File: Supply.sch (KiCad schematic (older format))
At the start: 22 parts, among them IC2 TPS65320C

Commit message: - removed 1 MOSFET of each group (no space) - removed 2 DC buffer caps (no space) - power stage routed - shunts and amps routed - post driver routed - pre driver HV routed
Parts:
- removed B1: MTC1, alexmod:MTC1, symbol MTC1
- removed C28: 22u, Capacitors_SMD:C_1206, symbol C
- removed C46: 5n6, Capacitors_SMD:C_0805, symbol C
- removed C47: 10u, Capacitors_SMD:C_0805, symbol C
- removed D8, D9: D_Schottky, Diodes_SMD:SMA_Standard, symbol D_Schottky
- removed IC2: TPS65320C, alexmod:TSSOP-14_4.4x5mm_Pitch0.65mm_EP, symbol TPS65320C
- added C10: 22u, Capacitors_SMD:C_0805, symbol C
- added C11, C12: 100n, Capacitors_SMD:C_0805, symbol C
- added C28: 100n, Capacitors_SMD:C_0805, symbol C_Small
- added C46: 3n3, Capacitors_SMD:C_0805, symbol C_Small
- added D8: 4148, Diodes_SMD:D_MiniMELF_Standard, symbol D_Small
- added IC1: LM5017, Housings_SOIC:SOIC-8-1EP_3.9x4.9mm_Pitch1.27mm, symbol LM5017
- added IC2: AP65111, TO_SOT_Packages_SMD:SOT-23-6, symbol AP65111
- added L2: NRH2410T100MN, alexmod:NRH2410, symbol INDUCTOR_SMALL
- added R30: 76k, Resistors_SMD:R_0805, symbol R
- added R31: 10k, Resistors_SMD:R_0805, symbol R
- added R49: 13k, Resistors_SMD:R_0805, symbol R
- added U6: 7805_SO8, Housings_SOIC:SOIC-8_3.9x4.9mm_Pitch1.27mm, symbol 7805_SO8
- C27: value 22u -> 100n; footprint Capacitors_SMD:C_1206 -> Capacitors_SMD:C_0805
- C29: value 100u 16V -> 47u 120V; footprint Capacitors_ThroughHole:C_Radial_D6.3_L11.2_P2.5 -> Capacitors_THT:CP_Radial_D6.3mm_P2.50mm
- C31: value 3n3 -> 100n
- C45: value 10p -> 22u
- C48: value 10u -> 22u
- C49: value 100u 6V3 -> 100u 22V; footprint Capacitors_ThroughHole:C_Radial_D6.3_L11.2_P2.5 -> Capacitors_THT:CP_Radial_D6.3mm_P2.50mm
- L1: value SRR6038-3R3Y -> VLS6045EX-221M; footprint alexmod:SRR6038 -> alexmod:VLS6045EX
- R39: value 52k3 -> 499k
- R40: value 28k -> 59k
- R41: value 30k1 -> 46k4
- R42: value 95k3 -> 40k2
- R43: value 18k2 -> 1k
- R44: value 95k3 -> 10k
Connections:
- net labels removed: +12VA, Earth, NRST
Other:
- moved on the sheet: C29, C30, C31, C32, C48, C49, L1, R43, R44

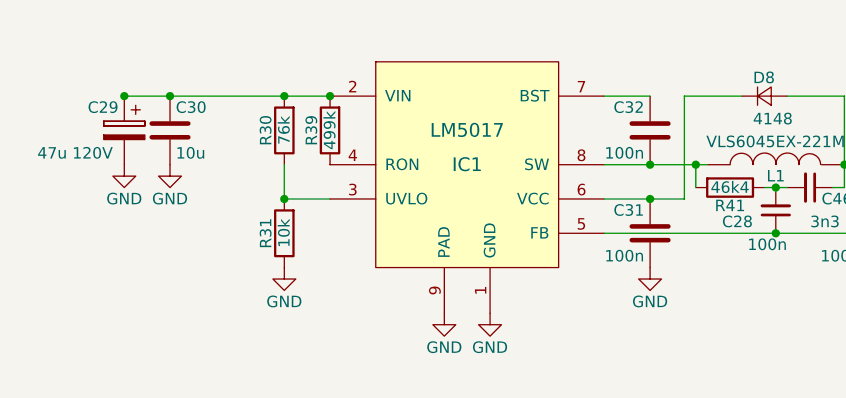
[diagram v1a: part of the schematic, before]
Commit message: - redesigned the MOSFET mounting -> minor changes to the power stage - logic and interface routed -> layout finished - needs final check and gerber export
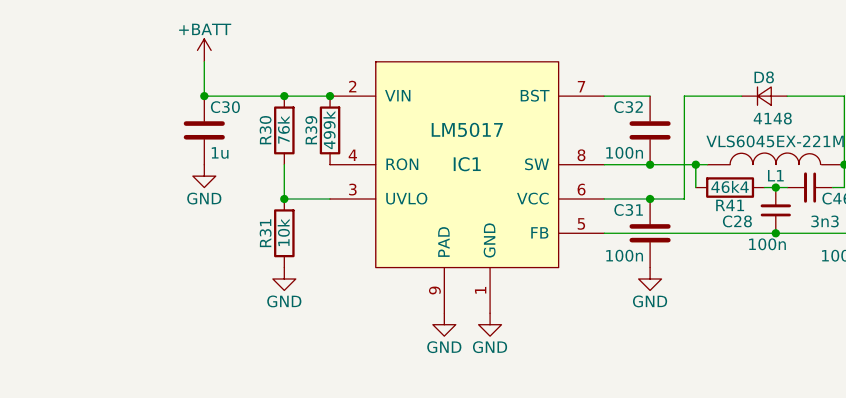
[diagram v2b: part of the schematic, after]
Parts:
- removed C29: 47u 120V, Capacitors_THT:CP_Radial_D6.3mm_P2.50mm, symbol CP
- C30: value 10u -> 1u; footprint Capacitors_SMD:C_0805 -> Capacitors_SMD:C_1206
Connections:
- net +BATT: now reaches C30.1, IC1.2 (VIN), R30.2, R39.2
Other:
- moved on the sheet: C30
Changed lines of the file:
@@
 L C C30
 U 1 1 589B52B3
-P 3750 1600
-F 0 "C30" H 3775 1700 50  0000 L CNN
-F 1 "10u" H 3775 1500 50  0000 L CNN
-F 2 "Capacitors_SMD:C_0805" H 3788 1450 50  0001 C CNN
-F 3 "" H 3750 1600 50  0000 C CNN
-	1    3750 1600
-	1    0    0    -1
-$EndComp
-$Comp
-L CP C29
-U 1 1 589B52D8
-P 3550 1600
-F 0 "C29" H 3575 1700 50  0000 L CNN
-F 1 "47u 120V" H 3600 1500 50  0000 L CNN
-F 2 "Capacitors_THT:CP_Radial_D6.3mm_P2.50mm" H 3588 1450 50  0001 C CNN
-F 3 "" H 3550 1600 50  0000 C CNN
-	1    3550 1600
-	-1   0    0    -1
+P 3900 1600
+F 0 "C30" H 3925 1700 50  0000 L CNN
+F 1 "1u" H 3925 1500 50  0000 L CNN
+F 2 "Capacitors_SMD:C_1206" H 3938 1450 50  0001 C CNN
+F 3 "" H 3900 1600 50  0000 C CNN
+	1    3900 1600
+	1    0    0    -1
 $EndComp
 $Comp
@@
 Connection ~ 7500 1750
 Wire Wire Line
-	3550 1450 4450 1450
-Connection ~ 3750 1450
-Connection ~ 3550 1450
+	3900 1450 4450 1450
+Connection ~ 3900 1450
 $Comp
 L GND #PWR054
 U 1 1 59A204D9
-P 3750 1750
-F 0 "#PWR054" H 3750 1500 50  0001 C CNN
-F 1 "GND" H 3750 1600 50  0000 C CNN
-F 2 "" H 3750 1750 60  0000 C CNN
-F 3 "" H 3750 1750 60  0000 C CNN
-	1    3750 1750
+P 3900 1750
+F 0 "#PWR054" H 3900 1500 50  0001 C CNN
+F 1 "GND" H 3900 1600 50  0000 C CNN
+F 2 "" H 3900 1750 60  0000 C CNN
+F 3 "" H 3900 1750 60  0000 C CNN
+	1    3900 1750
 	1    0    0    -1
 $EndComp
 $Comp
 L GND #PWR055
-U 1 1 59A20552
-P 3550 1750
-F 0 "#PWR055" H 3550 1500 50  0001 C CNN
-F 1 "GND" H 3550 1600 50  0000 C CNN
-F 2 "" H 3550 1750 60  0000 C CNN
-F 3 "" H 3550 1750 60  0000 C CNN
-	1    3550 1750
-	1    0    0    -1
-$EndComp
-$Comp
-L GND #PWR056
 U 1 1 59A20BA8
 P 5150 2400
-F 0 "#PWR056" H 5150 2150 50  0001 C CNN
+F 0 "#PWR055" H 5150 2150 50  0001 C CNN
 F 1 "GND" H 5150 2250 50  0000 C CNN
 F 2 "" H 5150 2400 60  0000 C CNN
@@
 Connection ~ 4450 1450
 $Comp
-L GND #PWR057
+L GND #PWR056
 U 1 1 59A21253
 P 4950 2400
-F 0 "#PWR057" H 4950 2150 50  0001 C CNN
+F 0 "#PWR056" H 4950 2150 50  0001 C CNN
 F 1 "GND" H 4950 2250 50  0000 C CNN
 F 2 "" H 4950 2400 60  0000 C CNN
@@
 	4250 1900 4450 1900
 $Comp
-L GND #PWR058
+L GND #PWR057
 U 1 1 59A21882
 P 4250 2200
-F 0 "#PWR058" H 4250 1950 50  0001 C CNN
+F 0 "#PWR057" H 4250 1950 50  0001 C CNN
 F 1 "GND" H 4250 2050 50  0000 C CNN
 F 2 "" H 4250 2200 60  0000 C CNN
@@
 	6250 1450 6000 1450
 Wire Wire Line
-	6000 1450 6000 1900
-Wire Wire Line
-	6000 1900 5650 1900
+	6000 1900 6000 1450
+Wire Wire Line
+	5650 1900 6000 1900
 $Comp
 L AP65111 IC2
@@
 $EndComp
 $Comp
-L +12V #PWR059
+L +12V #PWR058
 U 1 1 59A25AAF
 P 4300 3500
-F 0 "#PWR059" H 4300 3350 50  0001 C CNN
+F 0 "#PWR058" H 4300 3350 50  0001 C CNN
 F 1 "+12V" H 4300 3640 50  0000 C CNN
 F 2 "" H 4300 3500 60  0000 C CNN
@@
 Connection ~ 4300 3600
 $Comp
-L GND #PWR060
+L GND #PWR059
 U 1 1 59A26187
 P 4300 3900
-F 0 "#PWR060" H 4300 3650 50  0001 C CNN
+F 0 "#PWR059" H 4300 3650 50  0001 C CNN
 F 1 "GND" H 4300 3750 50  0000 C CNN
 F 2 "" H 4300 3900 60  0000 C CNN
@@
 $EndComp
 $Comp
-L GND #PWR061
+L GND #PWR060
 U 1 1 59A26636
 P 5050 4200
-F 0 "#PWR061" H 5050 3950 50  0001 C CNN
+F 0 "#PWR060" H 5050 3950 50  0001 C CNN
 F 1 "GND" H 5050 4050 50  0000 C CNN
 F 2 "" H 5050 4200 50  0000 C CNN
@@
 $EndComp
 $Comp
-L GND #PWR062
+L GND #PWR061
 U 1 1 59A2668D
 P 6200 4200
-F 0 "#PWR062" H 6200 3950 50  0001 C CNN
+F 0 "#PWR061" H 6200 3950 50  0001 C CNN
 F 1 "GND" H 6200 4050 50  0000 C CNN
 F 2 "" H 6200 4200 50  0000 C CNN
@@
 $EndComp
 $Comp
-L GND #PWR063
+L GND #PWR062
 U 1 1 59A26802
 P 6500 4200
-F 0 "#PWR063" H 6500 3950 50  0001 C CNN
+F 0 "#PWR062" H 6500 3950 50  0001 C CNN
 F 1 "GND" H 6500 4050 50  0000 C CNN
 F 2 "" H 6500 4200 50  0000 C CNN
@@
 Connection ~ 5500 3600
 $Comp
-L +3V3 #PWR064
+L +3V3 #PWR063
 U 1 1 59A27760
 P 6500 3500
-F 0 "#PWR064" H 6500 3350 50  0001 C CNN
+F 0 "#PWR063" H 6500 3350 50  0001 C CNN
 F 1 "+3V3" H 6500 3640 50  0000 C CNN
 F 2 "" H 6500 3500 50  0000 C CNN
@@
 Connection ~ 6500 3600
 $Comp
-L +12V #PWR065
+L +12V #PWR064
 U 1 1 59A27DFE
 P 4600 5050
-F 0 "#PWR065" H 4600 4900 50  0001 C CNN
+F 0 "#PWR064" H 4600 4900 50  0001 C CNN
 F 1 "+12V" H 4600 5190 50  0000 C CNN
 F 2 "" H 4600 5050 60  0000 C CNN
@@
 Connection ~ 4600 5150
 $Comp
-L GND #PWR066
+L GND #PWR065
 U 1 1 59A27E0D
 P 4600 5450
-F 0 "#PWR066" H 4600 5200 50  0001 C CNN
+F 0 "#PWR065" H 4600 5200 50  0001 C CNN
 F 1 "GND" H 4600 5300 50  0000 C CNN
 F 2 "" H 4600 5450 60  0000 C CNN
@@
 Connection ~ 5550 5150
 $Comp
-L GND #PWR067
+L GND #PWR066
 U 1 1 59A2862B
 P 5550 5450
-F 0 "#PWR067" H 5550 5200 50  0001 C CNN
+F 0 "#PWR066" H 5550 5200 50  0001 C CNN
 F 1 "GND" H 5550 5300 50  0000 C CNN
 F 2 "" H 5550 5450 60  0000 C CNN
@@
 $EndComp
 $Comp
-L GND #PWR068
+L GND #PWR067
 U 1 1 59A28C15
 P 5100 5450
-F 0 "#PWR068" H 5100 5200 50  0001 C CNN
+F 0 "#PWR067" H 5100 5200 50  0001 C CNN
 F 1 "GND" H 5100 5300 50  0000 C CNN
 F 2 "" H 5100 5450 60  0000 C CNN
@@
 $EndComp
 $Comp
-L GND #PWR069
+L GND #PWR068
 U 1 1 59BF9EB5
 P 4950 5450
-F 0 "#PWR069" H 4950 5200 50  0001 C CNN
+F 0 "#PWR068" H 4950 5200 50  0001 C CNN
 F 1 "GND" H 4950 5300 50  0000 C CNN
 F 2 "" H 4950 5450 60  0000 C CNN
@@
 $EndComp
 $Comp
-L GND #PWR070
+L GND #PWR069
 U 1 1 59BF9F14
 P 5000 5450
-F 0 "#PWR070" H 5000 5200 50  0001 C CNN
+F 0 "#PWR069" H 5000 5200 50  0001 C CNN
 F 1 "GND" H 5000 5300 50  0000 C CNN
 F 2 "" H 5000 5450 60  0000 C CNN
@@
 $EndComp
 $Comp
-L GND #PWR071
+L GND #PWR070
 U 1 1 59BFA02F
 P 5150 5450
-F 0 "#PWR071" H 5150 5200 50  0001 C CNN
+F 0 "#PWR070" H 5150 5200 50  0001 C CNN
 F 1 "GND" H 5150 5300 50  0000 C CNN
 F 2 "" H 5150 5450 60  0000 C CNN
@@
 	-1   0    0    -1
 $EndComp
+$Comp
+L +BATT #PWR071
+U 1 1 59C14A31
+P 3900 1300
+F 0 "#PWR071" H 3900 1150 50  0001 C CNN
+F 1 "+BATT" H 3900 1440 50  0000 C CNN
+F 2 "" H 3900 1300 50  0000 C CNN
+F 3 "" H 3900 1300 50  0000 C CNN
+	1    3900 1300
+	1    0    0    -1
+$EndComp
+Wire Wire Line
+	3900 1300 3900 1450
 $EndSCHEMATC

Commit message: - final check - minor layout cleanups - labeling - first production run => V1.0
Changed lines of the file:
@@
 	6250 1450 6000 1450
 Wire Wire Line
-	6000 1900 6000 1450
+	6000 1450 6000 1900
 Wire Wire Line
-	5650 1900 6000 1900
+	6000 1900 5650 1900
 $Comp
 L AP65111 IC2

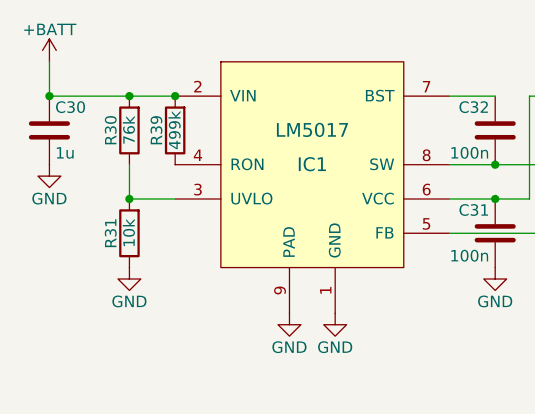
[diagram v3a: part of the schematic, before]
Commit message: - fixed swapped pins 2 and 3 on IC2 - added optional dividers to ADC inputs - made Vcc selectable between 3V3 or 5V
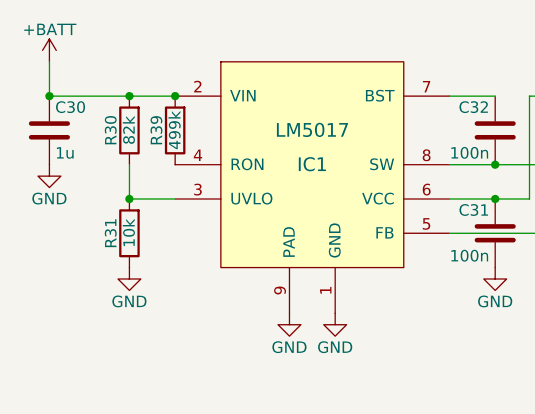
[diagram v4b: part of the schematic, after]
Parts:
- R30: value 76k -> 82k
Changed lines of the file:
@@
 $EndDescr
 $Comp
-L +12V #PWR048
+L +12V #PWR051
 U 1 1 5757C6C9
 P 7500 1650
-F 0 "#PWR048" H 7500 1500 50  0001 C CNN
+F 0 "#PWR051" H 7500 1500 50  0001 C CNN
 F 1 "+12V" H 7500 1790 50  0000 C CNN
 F 2 "" H 7500 1650 60  0000 C CNN
@@
 $EndComp
 $Comp
-L GND #PWR049
+L GND #PWR052
 U 1 1 589B6D8B
 P 5850 2200
-F 0 "#PWR049" H 5850 1950 50  0001 C CNN
+F 0 "#PWR052" H 5850 1950 50  0001 C CNN
 F 1 "GND" H 5850 2050 50  0000 C CNN
 F 2 "" H 5850 2200 60  0000 C CNN
@@
 $EndComp
 $Comp
-L +5V #PWR050
+L +5V #PWR053
 U 1 1 589BAA8C
 P 5550 5050
-F 0 "#PWR050" H 5550 4900 50  0001 C CNN
+F 0 "#PWR053" H 5550 4900 50  0001 C CNN
 F 1 "+5V" H 5550 5190 50  0000 C CNN
 F 2 "" H 5550 5050 50  0000 C CNN
@@
 Connection ~ 6950 1750
 $Comp
-L GND #PWR051
+L GND #PWR054
 U 1 1 59A1EBF8
 P 6950 2200
-F 0 "#PWR051" H 6950 1950 50  0001 C CNN
+F 0 "#PWR054" H 6950 1950 50  0001 C CNN
 F 1 "GND" H 6950 2050 50  0000 C CNN
 F 2 "" H 6950 2200 60  0000 C CNN
@@
 $EndComp
 $Comp
-L GND #PWR052
+L GND #PWR055
 U 1 1 59A1EC3C
 P 7200 2200
-F 0 "#PWR052" H 7200 1950 50  0001 C CNN
+F 0 "#PWR055" H 7200 1950 50  0001 C CNN
 F 1 "GND" H 7200 2050 50  0000 C CNN
 F 2 "" H 7200 2200 60  0000 C CNN
@@
 $EndComp
 $Comp
-L GND #PWR053
+L GND #PWR056
 U 1 1 59A1F45A
 P 7500 2350
-F 0 "#PWR053" H 7500 2100 50  0001 C CNN
+F 0 "#PWR056" H 7500 2100 50  0001 C CNN
 F 1 "GND" H 7500 2200 50  0000 C CNN
 F 2 "" H 7500 2350 60  0000 C CNN
@@
 Connection ~ 3900 1450
 $Comp
-L GND #PWR054
+L GND #PWR057
 U 1 1 59A204D9
 P 3900 1750
-F 0 "#PWR054" H 3900 1500 50  0001 C CNN
+F 0 "#PWR057" H 3900 1500 50  0001 C CNN
 F 1 "GND" H 3900 1600 50  0000 C CNN
 F 2 "" H 3900 1750 60  0000 C CNN
@@
 $EndComp
 $Comp
-L GND #PWR055
+L GND #PWR058
 U 1 1 59A20BA8
 P 5150 2400
-F 0 "#PWR055" H 5150 2150 50  0001 C CNN
+F 0 "#PWR058" H 5150 2150 50  0001 C CNN
 F 1 "GND" H 5150 2250 50  0000 C CNN
 F 2 "" H 5150 2400 60  0000 C CNN
@@
 Connection ~ 4450 1450
 $Comp
-L GND #PWR056
+L GND #PWR059
 U 1 1 59A21253
 P 4950 2400
-F 0 "#PWR056" H 4950 2150 50  0001 C CNN
+F 0 "#PWR059" H 4950 2150 50  0001 C CNN
 F 1 "GND" H 4950 2250 50  0000 C CNN
 F 2 "" H 4950 2400 60  0000 C CNN
@@
 P 4250 1600
 F 0 "R30" V 4330 1600 50  0000 C CNN
-F 1 "76k" V 4250 1600 50  0000 C CNN
+F 1 "82k" V 4250 1600 50  0000 C CNN
 F 2 "Resistors_SMD:R_0805" V 4180 1600 50  0001 C CNN
 F 3 "" H 4250 1600 50  0000 C CNN
@@
 	4250 1900 4450 1900
 $Comp
-L GND #PWR057
+L GND #PWR060
 U 1 1 59A21882
 P 4250 2200
-F 0 "#PWR057" H 4250 1950 50  0001 C CNN
+F 0 "#PWR060" H 4250 1950 50  0001 C CNN
 F 1 "GND" H 4250 2050 50  0000 C CNN
 F 2 "" H 4250 2200 60  0000 C CNN
@@
 	6000 1900 5650 1900
 $Comp
-L AP65111 IC2
-U 1 1 59A255A2
-P 5050 3600
-F 0 "IC2" H 5050 3500 60  0000 C CNN
-F 1 "AP65111" H 5050 3750 60  0000 C CNN
-F 2 "TO_SOT_Packages_SMD:SOT-23-6" H 5050 3400 60  0001 C CNN
-F 3 "" H 5050 3400 60  0000 C CNN
-	1    5050 3600
-	1    0    0    -1
-$EndComp
-$Comp
-L +12V #PWR058
+L +12V #PWR061
 U 1 1 59A25AAF
 P 4300 3500
-F 0 "#PWR058" H 4300 3350 50  0001 C CNN
+F 0 "#PWR061" H 4300 3350 50  0001 C CNN
 F 1 "+12V" H 4300 3640 50  0000 C CNN
 F 2 "" H 4300 3500 60  0000 C CNN
@@
 Connection ~ 4300 3600
 $Comp
-L GND #PWR059
+L GND #PWR062
 U 1 1 59A26187
 P 4300 3900
-F 0 "#PWR059" H 4300 3650 50  0001 C CNN
+F 0 "#PWR062" H 4300 3650 50  0001 C CNN
 F 1 "GND" H 4300 3750 50  0000 C CNN
 F 2 "" H 4300 3900 60  0000 C CNN
@@
 $EndComp
 $Comp
-L GND #PWR060
+L GND #PWR063
 U 1 1 59A26636
 P 5050 4200
-F 0 "#PWR060" H 5050 3950 50  0001 C CNN
+F 0 "#PWR063" H 5050 3950 50  0001 C CNN
 F 1 "GND" H 5050 4050 50  0000 C CNN
 F 2 "" H 5050 4200 50  0000 C CNN
@@
 $EndComp
 $Comp
-L GND #PWR061
+L GND #PWR064
 U 1 1 59A2668D
 P 6200 4200
-F 0 "#PWR061" H 6200 3950 50  0001 C CNN
+F 0 "#PWR064" H 6200 3950 50  0001 C CNN
 F 1 "GND" H 6200 4050 50  0000 C CNN
 F 2 "" H 6200 4200 50  0000 C CNN
@@
 $EndComp
 $Comp
-L GND #PWR062
+L GND #PWR065
 U 1 1 59A26802
 P 6500 4200
-F 0 "#PWR062" H 6500 3950 50  0001 C CNN
+F 0 "#PWR065" H 6500 3950 50  0001 C CNN
 F 1 "GND" H 6500 4050 50  0000 C CNN
 F 2 "" H 6500 4200 50  0000 C CNN
@@
 Connection ~ 5500 3600
 $Comp
-L +3V3 #PWR063
+L +3V3 #PWR066
 U 1 1 59A27760
 P 6500 3500
-F 0 "#PWR063" H 6500 3350 50  0001 C CNN
+F 0 "#PWR066" H 6500 3350 50  0001 C CNN
 F 1 "+3V3" H 6500 3640 50  0000 C CNN
 F 2 "" H 6500 3500 50  0000 C CNN
@@
 Connection ~ 6500 3600
 $Comp
-L +12V #PWR064
+L +12V #PWR067
 U 1 1 59A27DFE
 P 4600 5050
-F 0 "#PWR064" H 4600 4900 50  0001 C CNN
+F 0 "#PWR067" H 4600 4900 50  0001 C CNN
 F 1 "+12V" H 4600 5190 50  0000 C CNN
 F 2 "" H 4600 5050 60  0000 C CNN
@@
 Connection ~ 4600 5150
 $Comp
-L GND #PWR065
+L GND #PWR068
 U 1 1 59A27E0D
 P 4600 5450
-F 0 "#PWR065" H 4600 5200 50  0001 C CNN
+F 0 "#PWR068" H 4600 5200 50  0001 C CNN
 F 1 "GND" H 4600 5300 50  0000 C CNN
 F 2 "" H 4600 5450 60  0000 C CNN
@@
 Connection ~ 5550 5150
 $Comp
-L GND #PWR066
+L GND #PWR069
 U 1 1 59A2862B
 P 5550 5450
-F 0 "#PWR066" H 5550 5200 50  0001 C CNN
+F 0 "#PWR069" H 5550 5200 50  0001 C CNN
 F 1 "GND" H 5550 5300 50  0000 C CNN
 F 2 "" H 5550 5450 60  0000 C CNN
@@
 $EndComp
 $Comp
-L GND #PWR067
+L GND #PWR070
 U 1 1 59A28C15
 P 5100 5450
-F 0 "#PWR067" H 5100 5200 50  0001 C CNN
+F 0 "#PWR070" H 5100 5200 50  0001 C CNN
 F 1 "GND" H 5100 5300 50  0000 C CNN
 F 2 "" H 5100 5450 60  0000 C CNN
@@
 $EndComp
 $Comp
-L GND #PWR068
+L GND #PWR071
 U 1 1 59BF9EB5
 P 4950 5450
-F 0 "#PWR068" H 4950 5200 50  0001 C CNN
+F 0 "#PWR071" H 4950 5200 50  0001 C CNN
 F 1 "GND" H 4950 5300 50  0000 C CNN
 F 2 "" H 4950 5450 60  0000 C CNN
@@
 $EndComp
 $Comp
-L GND #PWR069
+L GND #PWR072
 U 1 1 59BF9F14
 P 5000 5450
-F 0 "#PWR069" H 5000 5200 50  0001 C CNN
+F 0 "#PWR072" H 5000 5200 50  0001 C CNN
 F 1 "GND" H 5000 5300 50  0000 C CNN
 F 2 "" H 5000 5450 60  0000 C CNN
@@
 $EndComp
 $Comp
-L GND #PWR070
+L GND #PWR073
 U 1 1 59BFA02F
 P 5150 5450
-F 0 "#PWR070" H 5150 5200 50  0001 C CNN
+F 0 "#PWR073" H 5150 5200 50  0001 C CNN
 F 1 "GND" H 5150 5300 50  0000 C CNN
 F 2 "" H 5150 5450 60  0000 C CNN
@@
 $EndComp
 $Comp
-L +BATT #PWR071
+L +BATT #PWR074
 U 1 1 59C14A31
 P 3900 1300
-F 0 "#PWR071" H 3900 1150 50  0001 C CNN
+F 0 "#PWR074" H 3900 1150 50  0001 C CNN
 F 1 "+BATT" H 3900 1440 50  0000 C CNN
 F 2 "" H 3900 1300 50  0000 C CNN
@@
 Wire Wire Line
 	3900 1300 3900 1450
+$Comp
+L AP65111 IC2
+U 1 1 5A89C59A
+P 5050 3600
+F 0 "IC2" H 5050 3500 60  0000 C CNN
+F 1 "AP65111" H 5050 3750 60  0000 C CNN
+F 2 "TO_SOT_Packages_SMD:SOT-23-6" H 5050 3400 60  0001 C CNN
+F 3 "" H 5050 3400 60  0000 C CNN
+	1    5050 3600
+	1    0    0    -1
+$EndComp
 $EndSCHEMATC
